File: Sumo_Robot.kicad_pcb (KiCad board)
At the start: 4 copper layers, 90 x 90 mm, 65 parts, among them J10 Screw_Terminal_01x03, J12 Screw_Terminal_01x02, J14 Screw_Terminal_01x02, J15 Conn_01x02, J16 Conn_01x03, J17 Conn_01x08, J18 Conn_01x02, J19 Conn_01x02, J2 Screw_Terminal_01x04, J3 Screw_Terminal_01x04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

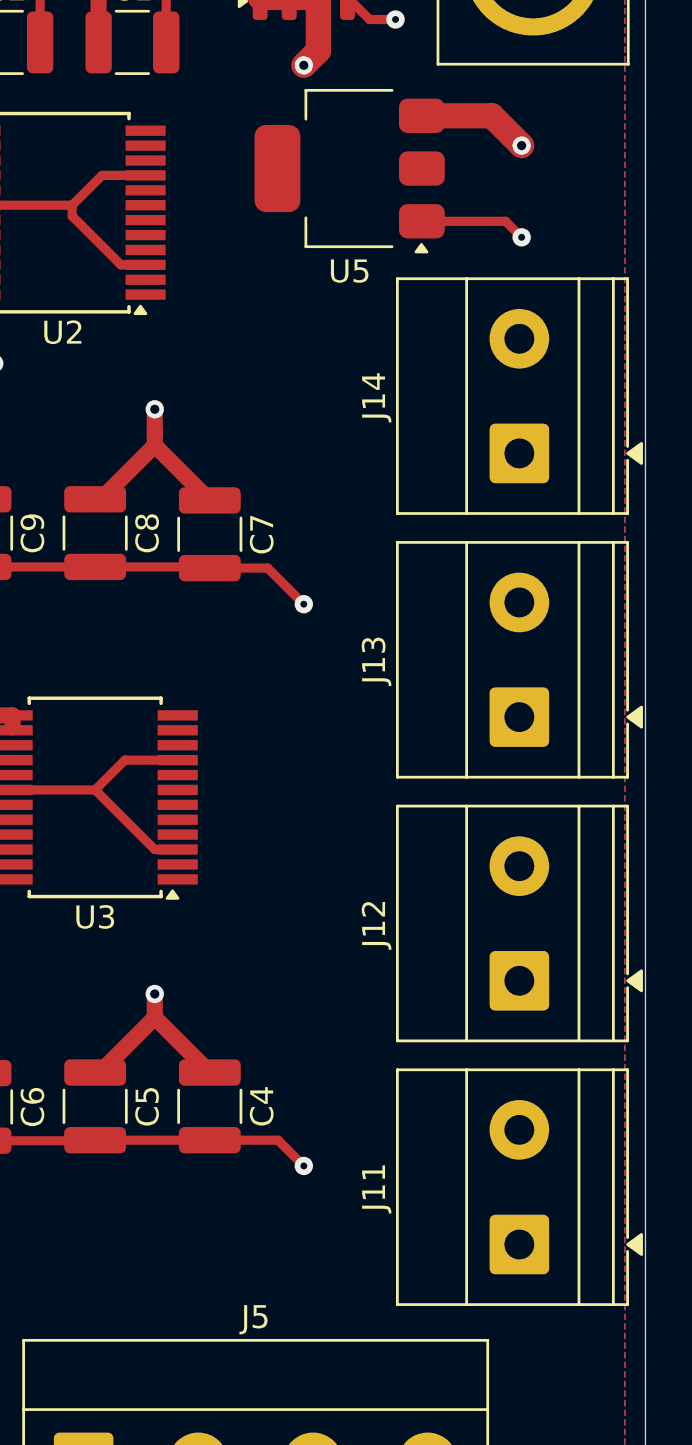
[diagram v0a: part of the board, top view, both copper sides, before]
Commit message: updated layout
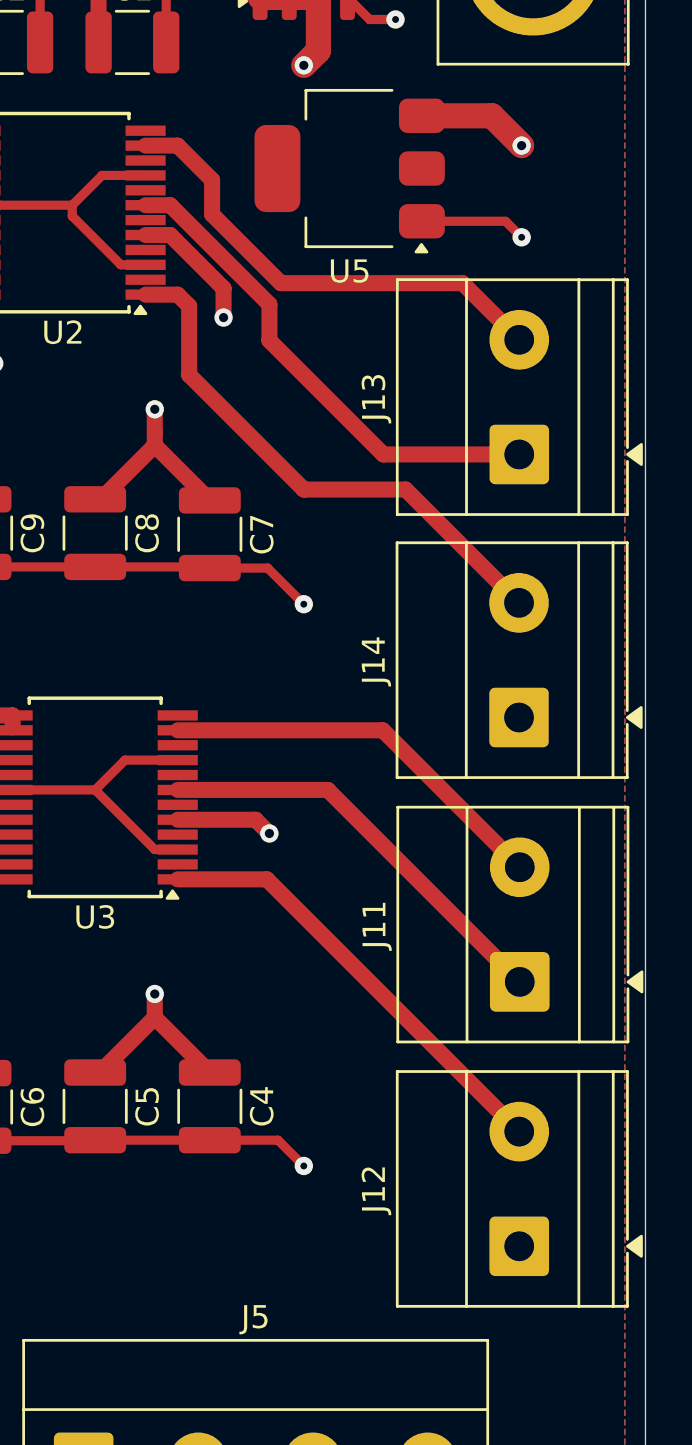
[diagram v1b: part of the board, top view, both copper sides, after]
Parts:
- moved J12 11.6 mm to (188.4, 112.5)
- moved J14 11.5 mm to (188.4, 89.4)
- moved J13 11.5 mm to (188.4, 78.0)
- moved J11 11.5 mm to (188.4, 101.0)
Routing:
- net MR_A02: track 0.00 -> 29.0 mm, vias 0 -> 1
- net ML_A02: track 1.27 -> 27.3 mm, vias 0 -> 1
- net MR_A01: track 0.00 -> 23.6 mm
- net MR_B02: track 0.00 -> 21.7 mm
- net MR_B01: track 0.00 -> 20.7 mm
- net ML_A01: track 0.00 -> 19.5 mm
- net ML_B02: track 0.00 -> 18.4 mm
- net ML_B01: track 0.00 -> 17.4 mm
- net UNUSED_1: track 11.5 -> 23.5 mm
- net UNUSED_2: track 20.7 -> 23.1 mm

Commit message: updating layout
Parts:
- moved J5 68.8 mm to (110.1, 87.0), turned to -90 degrees
- moved J18 59.3 mm to (133.3, 114.7)
- moved J10 55.2 mm to (114.1, 133.0), turned to 0 degrees
- moved J9 43.9 mm to (130.5, 132.9), turned to 0 degrees
- moved J6 40.1 mm to (110.1, 108.5), turned to -90 degrees
- moved J8 33.8 mm to (146.9, 132.9)
- moved J7 33.7 mm to (163.2, 132.9)
- moved J4 29.8 mm to (110.0, 65.6), turned to -90 degrees
- moved U2 27.5 mm to (147.1, 84.8)
- moved U5 27.5 mm to (159.6, 82.8)
- moved C7 23.8 mm to (160.0, 100.0)
- moved C8 23.8 mm to (155.0, 99.9)
- moved C9 23.8 mm to (150.0, 99.9)
- moved J2 22.1 mm to (157.8, 59.4)
- moved J3 22.1 mm to (136.3, 59.4)
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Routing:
- net /InfraredReceiver/IR_RECEIVE: track 88.4 -> 14.0 mm
- net MR_A01: track 23.6 -> 0.00 mm
- net MR_A02: track 29.0 -> 5.64 mm
- net ML_A02: track 27.3 -> 4.25 mm
- net MR_B02: track 21.7 -> 0.00 mm
- net MR_B01: track 20.7 -> 0.00 mm
- net UNUSED_1: track 23.5 -> 3.48 mm
- net ML_A01: track 19.5 -> 0.00 mm
- net ML_B02: track 18.4 -> 0.00 mm
- net ML_B01: track 17.4 -> 0.00 mm
- net GND: track 137.4 -> 126.0 mm, vias 15 -> 14
- net Net-(U6-Vs): track 13.1 -> 4.06 mm
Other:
- board size 90 x 90 mm -> 79.5 x 86 mm

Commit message: Layout updates
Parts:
- moved D2 53.4 mm to (167.5, 99.6), turned to 90 degrees
- moved R2 50.1 mm to (167.5, 94.0), turned to -90 degrees
- moved R8 31.1 mm to (120.0, 124.5), turned to 180 degrees
- moved D7 26.5 mm to (125.6, 124.5), turned to 180 degrees
- moved D5 26.3 mm to (153.4, 124.5)
- moved R6 26.3 mm to (147.8, 124.6)
- moved D4 26.0 mm to (165.9, 124.5)
- moved R5 26.0 mm to (160.3, 124.5)
- moved D6 21.9 mm to (137.9, 124.5), turned to 180 degrees
- moved R7 20.8 mm to (132.3, 124.5), turned to 180 degrees
- moved J16 5.71 mm to (144.5, 95.5)
- moved D9 4.31 mm to (121.5, 91.0)
- moved R11 4.31 mm to (121.6, 106.5)
- moved R12 4.31 mm to (121.6, 111.5)
- moved R9 4.31 mm to (121.5, 101.5)
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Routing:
- net ~{RST}: track 0.00 -> 36.7 mm
- net MR_B02: track 0.00 -> 28.7 mm, vias 0 -> 1
- net MR_A01: track 0.00 -> 27.7 mm
- net MR_B01: track 0.00 -> 27.2 mm, vias 0 -> 1
- net MR_A02: track 5.64 -> 30.9 mm
- net ML_A02: track 4.25 -> 22.1 mm
- net ML_A01: track 0.00 -> 16.5 mm
- net ML_B01: track 0.00 -> 15.8 mm
- net ML_B02: track 0.00 -> 15.4 mm
- net /LineSensors/LD_BACK_RIGHT: track 0.00 -> 13.2 mm
- net GND: track 126.0 -> 137.8 mm
- net /LineSensors/LD_FRONT_LEFT: track 0.00 -> 11.2 mm
- net +BATT: track 45.4 -> 55.4 mm
- net /LineSensors/LD_FRONT_RIGHT: track 0.00 -> 10.0 mm
- net /LineSensors/LD_BACK_LEFT: track 0.00 -> 9.63 mm
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
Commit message: updating layers
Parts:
- moved R13 7.02 mm to (140.6, 69.2)
- moved D8 4.24 mm to (144.5, 71.9)
- moved R7 2.54 mm to (132.7, 122.0)
- moved D7 2.54 mm to (126.1, 122.0)
- moved R8 2.54 mm to (120.5, 122.0)
- moved D6 2.54 mm to (138.4, 122.0)
- moved J15 1.53 mm to (145.0, 68.0)
- moved D4 0.50 mm to (165.9, 124.0)
- moved D5 0.50 mm to (153.4, 124.0)
- moved R5 0.50 mm to (160.3, 124.0)
- moved R6 0.50 mm to (147.8, 124.1)
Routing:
- net GND: track 137.8 -> 131.0 mm, vias 14 -> 13
- net Net-(D8-A): track 0.00 -> 3.92 mm
- net TEST_LED: track 6.32 -> 3.49 mm
- net /LineSensors/LD_BACK_RIGHT: track 13.2 -> 15.8 mm
- net /LineSensors/LD_FRONT_RIGHT: track 10.0 -> 12.7 mm
- net /LineSensors/LD_FRONT_LEFT: track 11.2 -> 12.0 mm
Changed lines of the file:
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@@
 	(footprint "LED_SMD:LED_1210_3225Metric"
 		(layer "F.Cu")
-		(at 145.771557 75.946975 90)
+		(at 144.5 71.9 90)
 		(descr "LED SMD 1210 (3225 Metric), square (rectangular) end terminal, IPC-7351 nominal, (Body size source: http://www.tortai-tech.com/upload/download/2011102023233369053.pdf), generated with kicad-footprint-generator")
 		(tags "LED")
 		(property "Reference" "D8"
-			(at 3.1 0.175 0)
+			(at 1.5 3 0)
 			(layer "F.SilkS")
 			(effects
@@
 		(tags "capacitor")
 		(property "Reference" "C12"
-			(at 0 -2.3 0)
+			(at -3.725 0.025 90)
 			(layer "F.SilkS")
 			(effects
@@
 	(footprint "LED_SMD:LED_1210_3225Metric"
 		(layer "F.Cu")
-		(at 125.6475 124.5 180)
+		(at 126.1 122 180)
 		(descr "LED SMD 1210 (3225 Metric), square (rectangular) end terminal, IPC-7351 nominal, (Body size source: http://www.tortai-tech.com/upload/download/2011102023233369053.pdf), generated with kicad-footprint-generator")
 		(tags "LED")
@@
 	(footprint "Resistor_SMD:R_1210_3225Metric"
 		(layer "F.Cu")
-		(at 132.29 124.5 180)
+		(at 132.7425 122 180)
 		(descr "Resistor SMD 1210 (3225 Metric), square (rectangular) end terminal, IPC-7351 nominal, (Body size source: IPC-SM-782 page 72, https://www.pcb-3d.com/wordpress/wp-content/uploads/ipc-sm-782a_amendment_1_and_2.pdf), generated with kicad-footprint-generator")
 		(tags "resistor")
@@
 	(footprint "Resistor_SMD:R_1210_3225Metric"
 		(layer "F.Cu")
-		(at 147.79 124.62 180)
+		(at 147.79 124.12 180)
 		(descr "Resistor SMD 1210 (3225 Metric), square (rectangular) end terminal, IPC-7351 nominal, (Body size source: IPC-SM-782 page 72, https://www.pcb-3d.com/wordpress/wp-content/uploads/ipc-sm-782a_amendment_1_and_2.pdf), generated with kicad-footprint-generator")
 		(tags "resistor")
@@
 	(footprint "Resistor_SMD:R_1210_3225Metric"
 		(layer "F.Cu")
-		(at 120.0375 124.5 180)
+		(at 120.49 122 180)
 		(descr "Resistor SMD 1210 (3225 Metric), square (rectangular) end terminal, IPC-7351 nominal, (Body size source: IPC-SM-782 page 72, https://www.pcb-3d.com/wordpress/wp-content/uploads/ipc-sm-782a_amendment_1_and_2.pdf), generated with kicad-footprint-generator")
 		(tags "resistor")
@@
 	(footprint "Resistor_SMD:R_1210_3225Metric"
 		(layer "F.Cu")
-		(at 142 76.05 -90)
+		(at 140.63681 69.167041 -90)
 		(descr "Resistor SMD 1210 (3225 Metric), square (rectangular) end terminal, IPC-7351 nominal, (Body size source: IPC-SM-782 page 72, https://www.pcb-3d.com/wordpress/wp-content/uploads/ipc-sm-782a_amendment_1_and_2.pdf), generated with kicad-footprint-generator")
 		(tags "resistor")
@@
 	(footprint "LED_SMD:LED_1210_3225Metric"
 		(layer "F.Cu")
-		(at 165.94 124.46 180)
+		(at 165.94 123.96 180)
 		(descr "LED SMD 1210 (3225 Metric), square (rectangular) end terminal, IPC-7351 nominal, (Body size source: http://www.tortai-tech.com/upload/download/2011102023233369053.pdf), generated with kicad-footprint-generator")
 		(tags "LED")
@@
 	(footprint "LED_SMD:LED_1210_3225Metric"
 		(layer "F.Cu")
-		(at 153.4 124.5 180)
+		(at 153.4 124 180)
 		(descr "LED SMD 1210 (3225 Metric), square (rectangular) end terminal, IPC-7351 nominal, (Body size source: http://www.tortai-tech.com/upload/download/2011102023233369053.pdf), generated with kicad-footprint-generator")
 		(tags "LED")
@@
 	(footprint "LED_SMD:LED_1210_3225Metric"
 		(layer "F.Cu")
-		(at 137.9 124.5 180)
+		(at 138.3525 122 180)
 		(descr "LED SMD 1210 (3225 Metric), square (rectangular) end terminal, IPC-7351 nominal, (Body size source: http://www.tortai-tech.com/upload/download/2011102023233369053.pdf), generated with kicad-footprint-generator")
 		(tags "LED")
@@
 	(footprint "Connector_PinHeader_1.00mm:PinHeader_1x02_P1.00mm_Vertical"
 		(layer "F.Cu")
-		(at 144.5 69.45 -90)
+		(at 145 68 -90)
 		(descr "Through hole straight pin header, 1x02, 1.00mm pitch, single row")
 		(tags "Through hole pin header THT 1x02 1.00mm single row")
@@
 	(footprint "Resistor_SMD:R_1210_3225Metric"
 		(layer "F.Cu")
-		(at 160.33 124.5 180)
+		(at 160.33 124 180)
 		(descr "Resistor SMD 1210 (3225 Metric), square (rectangular) end terminal, IPC-7351 nominal, (Body size source: IPC-SM-782 page 72, https://www.pcb-3d.com/wordpress/wp-content/uploads/ipc-sm-782a_amendment_1_and_2.pdf), generated with kicad-footprint-generator")
 		(tags "resistor")
@@
 	)
 	(segment
-		(start 145.771557 77.346975)
-		(end 148.346975 77.346975)
-		(width 0.2)
-		(layer "F.Cu")
-		(net 2)
-	)
-	(segment
 		(start 149.625 87.05)
 		(end 147.5 84.925)
@@
 	)
 	(segment
-		(start 144.5 69.45)
-		(end 145.55 69.45)
-		(width 0.2)
-		(layer "F.Cu")
-		(net 2)
-	)
-	(segment
 		(start 147.2 111.475)
 		(end 149.375 111.475)
@@
 	)
 	(segment
+		(start 140.475 94.25)
+		(end 139 94.25)
+		(width 0.2)
+		(layer "F.Cu")
+		(net 2)
+	)
+	(segment
+		(start 141.1 94.875)
+		(end 140.475 94.25)
+		(width 0.2)
+		(layer "F.Cu")
+		(net 2)
+	)
+	(segment
 		(start 122.875 91)
 		(end 122.875 87.375)
@@
 	)
 	(segment
-		(start 141.1 94.875)
-		(end 141.1 97.375)
-		(width 0.2)
-		(layer "F.Cu")
-		(net 2)
-	)
-	(segment
 		(start 151.7 109.15)
 		(end 154.1 109.15)
@@
 	)
 	(segment
-		(start 148.346975 77.346975)
-		(end 149.5 78.5)
-		(width 0.2)
-		(layer "F.Cu")
-		(net 2)
-	)
-	(segment
 		(start 153.5 119.475)
 		(end 158.475 119.475)
@@
 	)
 	(segment
-		(start 143.5 84.45)
-		(end 144.475 84.45)
-		(width 0.1)
-		(layer "F.Cu")
-		(net 2)
-	)
-	(segment
 		(start 155.05 101.45)
 		(end 155 101.4)
@@
 	)
 	(segment
-		(start 145.55 69.45)
-		(end 147.5 67.5)
-		(width 0.2)
-		(layer "F.Cu")
-		(net 2)
-	)
-	(segment
 		(start 153.5 119.475)
 		(end 150 115.975)
@@
 	)
 	(segment
-		(start 140.475 94.25)
+		(start 141.1 96.5)
 		(end 141.1 94.875)
 		(width 0.2)
@@
 	)
 	(segment
+		(start 147.5 73.4)
+		(end 147.4 73.3)
+		(width 0.2)
+		(layer "F.Cu")
+		(net 2)
+	)
+	(segment
 		(start 143.5 84.45)
 		(end 140.55 84.45)
@@
 	)
 	(segment
-		(start 139 94.25)
-		(end 140.475 94.25)
-		(width 0.2)
-		(layer "F.Cu")
-		(net 2)
-	)
-	(segment
 		(start 133.3125 84.05)
 		(end 131 84.05)
@@
 	)
 	(segment
+		(start 147.4 73.3)
+		(end 144.5 73.3)
+		(width 0.2)
+		(layer "F.Cu")
+		(net 2)
+	)
+	(segment
 		(start 133.8 79.5625)
 		(end 135.8 81.5625)
@@
 	)
 	(via
-		(at 141.1 97.375)
+		(at 141.1 96.5)
 		(size 0.8)
 		(drill 0.3)
@@
 	)
 	(via
-		(at 147.5 67.5)
-		(size 0.8)
-		(drill 0.3)
-		(layers "F.Cu" "B.Cu")
-		(remove_unused_layers yes)
-		(keep_end_layers no)
-		(zone_layer_connections "B.Cu")
-		(net 2)
-	)
-	(via
-		(at 149.5 78.5)
+		(at 147.5 73.4)
 		(size 0.8)
 		(drill 0.3)
@@
 	)
 	(segment
-		(start 168.96 124.46)
-		(end 167.34 124.46)
+		(start 169.46 123.96)
+		(end 167.34 123.96)
 		(width 0.2)
 		(layer "F.Cu")
@@
 	)
 	(segment
-		(start 170 125.5)
-		(end 168.96 124.46)
+		(start 170 124.5)
+		(end 169.46 123.96)
 		(width 0.2)
 		(layer "F.Cu")
@@
 	)
 	(segment
-		(start 170 131.160209)
-		(end 170 125.5)
+		(start 168.242784 132.917425)
+		(end 170 131.160209)
 		(width 0.2)
 		(layer "F.Cu")
@@
 	)
 	(segment
-		(start 168.242784 132.917425)
-		(end 170 131.160209)
+		(start 170 131.160209)
+		(end 170 124.5)
 		(width 0.2)
 		(layer "F.Cu")
@@
 	)
 	(segment
-		(start 161.7925 124.5)
-		(end 164.5 124.5)
+		(start 161.7925 124)
+		(end 164.5 124)
 		(width 0.2)
 		(layer "F.Cu")
@@
 	)
 	(segment
-		(start 164.5 124.5)
-		(end 164.54 124.46)
+		(start 164.5 124)
+		(end 164.54 123.96)
 		(width 0.2)
 		(layer "F.Cu")
@@
 	)
 	(segment
-		(start 151.88 124.62)
-		(end 152 124.5)
+		(start 151.88 124.12)
+		(end 152 124)
 		(width 0.2)
 		(layer "F.Cu")
@@
 	)
 	(segment
-		(start 149.2525 124.62)
-		(end 151.88 124.62)
+		(start 149.2525 124.12)
+		(end 151.88 124.12)
 		(width 0.2)
 		(layer "F.Cu")
@@
 	(segment
 		(start 135.5 132.95)
-		(end 139.3 129.15)
+		(end 139.7525 128.6975)
 		(width 0.2)
 		(layer "F.Cu")
@@
 	)
 	(segment
-		(start 139.3 129.15)
-		(end 139.3 124.5)
+		(start 139.7525 128.6975)
+		(end 139.7525 122)
 		(width 0.2)
 		(layer "F.Cu")
@@
 	)
 	(segment
-		(start 133.7525 124.5)
-		(end 136.5 124.5)
+		(start 134.205 122)
+		(end 136.9525 122)
 		(width 0.2)
 		(layer "F.Cu")
@@
 	)
 	(segment
-		(start 119.127554 132.952061)
-		(end 123.079615 129)
+		(start 123.579615 128.5)
+		(end 126 128.5)
 		(width 0.2)
 		(layer "F.Cu")
@@
 	)
 	(segment
-		(start 123.079615 129)
-		(end 125.5 129)
+		(start 127.5 127)
+		(end 127.5 122)
 		(width 0.2)
 		(layer "F.Cu")
@@
 	)
 	(segment
-		(start 125.5 129)
-		(end 127.0475 127.4525)
+		(start 119.127554 132.952061)
+		(end 123.579615 128.5)
 		(width 0.2)
 		(layer "F.Cu")
@@
 	)
 	(segment
-		(start 127.0475 127.4525)
-		(end 127.0475 124.5)
+		(start 126 128.5)
+		(end 127.5 127)
 		(width 0.2)
 		(layer "F.Cu")
@@
 	)
 	(segment
-		(start 121.5 124.5)
-		(end 124.2475 124.5)
+		(start 121.9525 122)
+		(end 124.7 122)
 		(width 0.2)
 		(layer "F.Cu")
@@
 	)
 	(segment
+		(start 140.63681 70.629541)
+		(end 144.370459 70.629541)
+		(width 0.2)
+		(layer "F.Cu")
+		(net 14)
+	)
+	(segment
+		(start 144.370459 70.629541)
+		(end 144.5 70.5)
+		(width 0.2)
+		(layer "F.Cu")
+		(net 14)
+	)
+	(segment
 		(start 162.75 80.55)
 		(end 165.8 80.55)
@@
 	)
 	(segment
-		(start 142.55 69.45)
-		(end 143.5 69.45)
-		(width 0.2)
-		(layer "F.Cu")
-		(net 21)
-	)
-	(segment
-		(start 142 74.5875)
-		(end 142 70)
+		(start 143.704541 67.704541)
+		(end 144 68)
 		(width 0.2)
 		(layer "F.Cu")
@@
 	)
 	(segment
-		(start 142 70)
-		(end 142.55 69.45)
+		(start 140.63681 67.704541)
+		(end 143.704541 67.704541)
 		(width 0.2)
 		(layer "F.Cu")
@@
 		(polygon
 			(pts
-				(xy 104.5 53.95) (xy 182.5 53.95) (xy 182.5 138.45) (xy 104.5 138.45)
+				(xy 104.5 54) (xy 182.5 54) (xy 182.5 138.5) (xy 104.5 138.5)
 			)
 		)

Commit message: rethinking the layout
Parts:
- removed J17: Conn_01x08, Connector_PinHeader_1.00mm:PinHeader_1x08_P1.00mm_Vertical
- moved J18 91.7 mm to (40.7, 108.1), turned to 180 degrees
- moved J19 90.8 mm to (46.7, 115.1), turned to -90 degrees
- moved U1 87.1 mm to (48.8, 107.5), turned to 90 degrees
- moved C11 86.8 mm to (58.9, 118.6)
- moved C3 86.8 mm to (47.0, 77.7)
- moved D5 86.8 mm to (66.6, 125.6)
- moved J1 86.8 mm to (90.0, 67.7)
- moved J10 86.8 mm to (27.3, 134.6)
- moved J14 86.8 mm to (89.6, 99.9)
- moved J2 86.8 mm to (71.0, 61.0)
- moved J3 86.8 mm to (49.5, 61.0)
- moved R3 86.8 mm to (51.0, 77.6)
- moved R4 86.8 mm to (43.0, 77.7)
- moved R5 86.8 mm to (73.5, 125.6)
- moved R7 86.8 mm to (45.9, 123.6)
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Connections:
- U1 pad 11: UNUSED_5 -> unconnected-(U1-P2.1/TA1.1-Pad11)
- U1 pad 12: UNUSED_6 -> unconnected-(U1-P2.2/TA1.1-Pad12)
- U1 pad 13: UNUSED_7 -> unconnected-(U1-P3.2/TA1.1-Pad13)
- U1 pad 14: UNUSED_8 -> unconnected-(U1-P3.3/TA1.2-Pad14)
- U1 pad 15: UNUSED_2 -> unconnected-(U1-P3.4/TA0.0-Pad15)
- U1 pad 16: UNUSED_1 -> unconnected-(U1-P2.3/TA1.0-Pad16)
- U1 pad 8: UNUSED_3 -> unconnected-(U1-P3.1/TA1.0-Pad8)
- U1 pad 9: UNUSED_4 -> unconnected-(U1-P3.0/TA0.2-Pad9)
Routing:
- net GND: track 131.0 -> 0.00 mm, vias 13 -> 0
- net +BATT: track 55.4 -> 0.00 mm, vias 9 -> 0
- net ~{RST}: track 36.7 -> 0.00 mm
- net MR_A02: track 30.9 -> 0.00 mm, vias 1 -> 0
- net MR_B02: track 28.7 -> 0.00 mm, vias 1 -> 0
- net MR_A01: track 27.7 -> 0.00 mm
- net MR_B01: track 27.2 -> 0.00 mm, vias 1 -> 0
- net UNUSED_2: track 23.1 -> 0.00 mm, vias 1 -> 0
- net ML_A02: track 22.1 -> 0.00 mm, vias 1 -> 0
- net /InfraredReceiver/IR_RECEIVE: track 21.2 -> 0.00 mm, vias 2 -> 0
- net ML_A01: track 16.5 -> 0.00 mm
- net Net-(J1-+): track 16.2 -> 0.00 mm
- net ML_B01: track 15.8 -> 0.00 mm
- net /LineSensors/LD_BACK_RIGHT: track 15.8 -> 0.00 mm
- net ML_B02: track 15.4 -> 0.00 mm
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
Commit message: layout rethinking
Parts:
- moved D5 163.3 mm to (229.8, 119.2)
- moved R7 163.3 mm to (209.1, 117.2)
- moved C1 163.3 mm to (235.7, 71.8)
- moved C10 163.3 mm to (207.4, 80.8)
- moved C11 163.3 mm to (222.1, 112.2)
- moved C12 163.3 mm to (222.1, 106.7)
- moved C2 163.3 mm to (230.2, 71.8)
- moved C3 163.3 mm to (210.2, 71.3)
- moved C4 163.3 mm to (239.9, 113.2)
- moved C5 163.3 mm to (234.9, 113.2)
- moved C6 163.3 mm to (229.9, 113.2)
- moved C7 163.3 mm to (236.4, 95.2)
- moved C8 163.3 mm to (231.4, 95.2)
- moved C9 163.3 mm to (226.4, 95.2)
- moved D1 163.3 mm to (236.1, 64.8)
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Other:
- board size 79.5 x 86 mm -> 78 x 84.5 mm

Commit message: updating pcb layout
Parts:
- removed J15: Conn_01x02, Connector_PinHeader_1.00mm:PinHeader_1x02_P1.00mm_Vertical
- moved D4 124.1 mm to (119.0, 105.8), turned to -90 degrees
- moved R2 120.6 mm to (125.0, 109.7), turned to 90 degrees
- moved D2 119.3 mm to (125.0, 104.1), turned to -90 degrees
- moved R5 118.0 mm to (119.0, 111.4), turned to -90 degrees
- moved U4 116.4 mm to (140.0, 121.2), turned to -90 degrees
- moved D5 114.6 mm to (118.9, 90.3), turned to -90 degrees
- moved C2 108.3 mm to (129.0, 110.2), turned to 90 degrees
- moved R6 107.8 mm to (119.0, 95.9), turned to -90 degrees
- moved U5 105.1 mm to (135.5, 108.7), turned to 90 degrees
- moved D6 105.0 mm to (119.0, 74.0), turned to -90 degrees
- moved D7 102.6 mm to (119.0, 57.5), turned to -90 degrees
- moved C1 101.8 mm to (141.5, 110.2), turned to 90 degrees
- moved C7 100.5 mm to (137.5, 77.2)
- moved C8 100.5 mm to (132.5, 77.2)
- moved C9 100.5 mm to (127.5, 77.2)
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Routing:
- net GND: track 0.00 -> 102.6 mm, vias 0 -> 26
- net Net-(U6-Vs): track 0.00 -> 9.85 mm
- net /InfraredReceiver/IR_RECEIVE: track 0.00 -> 5.72 mm
- net Net-(D3-A): track 0.00 -> 2.47 mm
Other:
- board size 78 x 84.5 mm -> 91 x 84.5 mm
